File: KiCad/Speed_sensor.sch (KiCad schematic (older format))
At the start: 69 parts, among them J1 USB_B_Micro, J2 SWD, U1 BQ24040DSQR, U2 TP1941U, U3 ST1PS02, U4 nRF52832-QFxx, U5 LIS2DH12, Y1 32,768kHz, Y2 32MHz

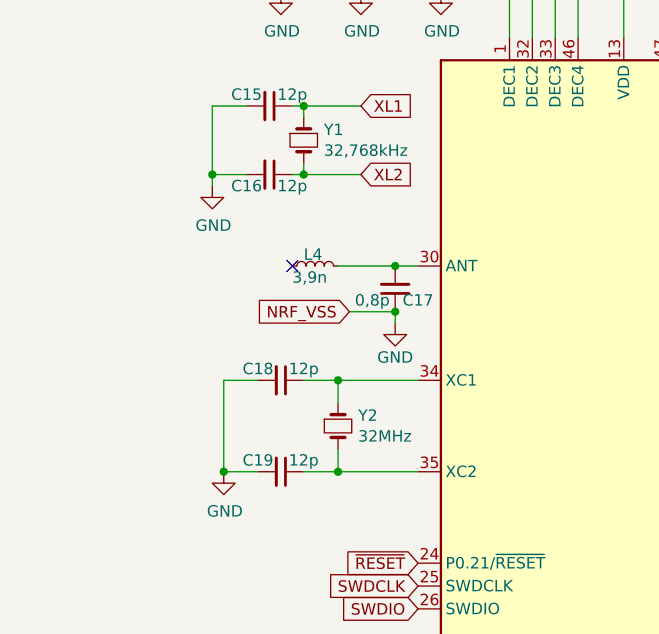
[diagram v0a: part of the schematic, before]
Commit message: added all footprints (LFO crystal might have to be updated)
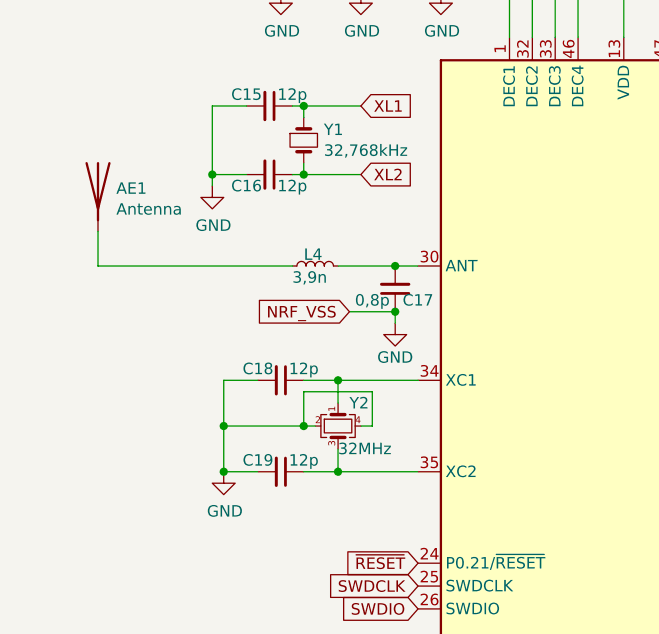
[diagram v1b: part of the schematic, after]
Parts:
- removed Y2: 32MHz, symbol Device:Crystal_Small
- added AE1: Antenna, RF_Antenna:Texas_SWRA117D_2.4GHz_Right, symbol Device:Antenna
- added Y2: 32MHz, Crystal:Crystal_SMD_2016-4Pin_2.0x1.6mm, symbol Device:Crystal_GND24_Small
- U1: footprint (none) -> Package_WSON-10:BQ24040DSQR_breitePins
- U2: footprint (none) -> Package_TO_SOT_SMD:SOT-23-5_HandSoldering
- U3: footprint (none) -> Package_TQFN-12:ST1PS02CQTR_breitePins
- U5: footprint (none) -> Package_LGA:LGA-12_2x2mm_P0.5mm
- Y1: footprint (none) -> Crystal:Crystal_SMD_2012-2Pin_2.0x1.2mm_HandSoldering
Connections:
- net GND: now also Y2.2, Y2.4
- net at C18.1, U4.34 (XC1): now also Y2.1
- net at C19.1, U4.35 (XC2): now also Y2.3
- net at L4.1: now also AE1.1 (A)
- no-connect marks 23 -> 22
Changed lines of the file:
@@
 Wire Wire Line
 	2500 3100 2850 3100
-$Comp
-L Device:Crystal_Small Y2
-U 1 1 6084A82A
-P 1900 5850
-F 0 "Y2" V 1854 5938 50  0000 L CNN
-F 1 "32MHz" V 1945 5938 50  0000 L CNN
-F 2 "" H 1900 5850 50  0001 C CNN
-F 3 "~" H 1900 5850 50  0001 C CNN
-	1    1900 5850
-	0    1    1    0
-$EndComp
 Wire Wire Line
 	2250 5650 1900 5650
@@
 	1550 5650 1400 5650
 Wire Wire Line
-	1400 5650 1400 6050
+	1400 5650 1400 5850
 Connection ~ 1400 6050
 $Comp
@@
 F 0 "U2" H 7950 1550 50  0000 C CNN
 F 1 "TP1941U" H 8000 1150 50  0000 C CNN
-F 2 "" H 8100 1350 50  0001 C CNN
+F 2 "Package_TO_SOT_SMD:SOT-23-5_HandSoldering" H 8100 1350 50  0001 C CNN
 F 3 "" H 8100 1350 50  0001 C CNN
 	1    8050 1350
@@
 F 0 "U3" H 9900 1600 50  0000 L CNN
 F 1 "ST1PS02" H 9900 800 50  0000 L CNN
-F 2 "" H 10150 1100 50  0001 C CNN
+F 2 "Package_TQFN-12:ST1PS02CQTR_breitePins" H 10150 1100 50  0001 C CNN
 F 3 "" H 10150 1100 50  0001 C CNN
 	1    10050 1200
@@
 F 0 "U1" H 3575 1915 50  0000 C CNN
 F 1 "BQ24040DSQR" H 3575 1824 50  0000 C CNN
-F 2 "" H 3550 1400 50  0001 C CNN
+F 2 "Package_WSON-10:BQ24040DSQR_breitePins" H 3550 1400 50  0001 C CNN
 F 3 "" H 3550 1400 50  0001 C CNN
 	1    3550 1400
@@
 F 0 "Y1" V 1704 4688 50  0000 L CNN
 F 1 "32,768kHz" V 1795 4688 50  0000 L CNN
-F 2 "" H 1750 4600 50  0001 C CNN
+F 2 "Crystal:Crystal_SMD_2012-2Pin_2.0x1.2mm_HandSoldering" H 1750 4600 50  0001 C CNN
 F 3 "~" H 1750 4600 50  0001 C CNN
 	1    1750 4600
@@
 F 0 "U5" H 7300 4750 50  0000 L CNN
 F 1 "LIS2DH12" H 7650 4750 50  0000 L CNN
-F 2 "" H 7550 4400 25  0001 C CNN
+F 2 "Package_LGA:LGA-12_2x2mm_P0.5mm" H 7550 4400 25  0001 C CNN
 F 3 "" H 7550 4400 25  0001 C CNN
 	1    7550 4400
@@
 Wire Wire Line
 	9000 1000 9000 1050
-NoConn ~ 1700 5150
 Wire Wire Line
 	3150 3050 3150 3100
@@
 Wire Wire Line
 	3150 3100 3150 4150
+$Comp
+L Device:Crystal_GND24_Small Y2
+U 1 1 6096B8F0
+P 1900 5850
+F 0 "Y2" V 1800 5900 50  0000 L CNN
+F 1 "32MHz" V 2000 5850 50  0000 L CNN
+F 2 "Crystal:Crystal_SMD_2016-4Pin_2.0x1.6mm" H 1900 5850 50  0001 C CNN
+F 3 "~" H 1900 5850 50  0001 C CNN
+	1    1900 5850
+	0    1    1    0
+$EndComp
+Wire Wire Line
+	1800 5850 1750 5850
+Connection ~ 1400 5850
+Wire Wire Line
+	1400 5850 1400 6050
+Connection ~ 1750 5850
+Wire Wire Line
+	1750 5850 1400 5850
+Wire Wire Line
+	1750 5700 1750 5850
+Wire Wire Line
+	2000 5850 2050 5850
+Wire Wire Line
+	2050 5850 2050 5700
+Wire Wire Line
+	1750 5700 2050 5700
+$Comp
+L Device:Antenna AE1
+U 1 1 6099647A
+P 850 4800
+F 0 "AE1" H 930 4789 50  0000 L CNN
+F 1 "Antenna" H 930 4698 50  0000 L CNN
+F 2 "RF_Antenna:Texas_SWRA117D_2.4GHz_Right" H 850 4800 50  0001 C CNN
+F 3 "~" H 850 4800 50  0001 C CNN
+	1    850  4800
+	1    0    0    -1
+$EndComp
+Wire Wire Line
+	850  5000 850  5150
+Wire Wire Line
+	850  5150 1700 5150
 $EndSCHEMATC

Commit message: custom footprints von Manu übernommen (jetzt sollte alles passen), PCB layout angefangen.
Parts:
- U4: footprint Package_DFN_QFN:QFN-48-1EP_6x6mm_P0.4mm_EP4.6x4.6mm -> myparts:QFN-48-1EP_6x6mm_P0.4mm_EP4.6x4.6mm_Handsolder
- U5: footprint Package_LGA:LGA-12_2x2mm_P0.5mm -> myparts:LGA-12_2x2mm_P0.5mm_Handsolder
- Y1: footprint Crystal:Crystal_SMD_2012-2Pin_2.0x1.2mm_HandSoldering -> myparts:TestPoint_2Pads_Pitch1mm_Drill0.4mm
- Y2: footprint Crystal:Crystal_SMD_2016-4Pin_2.0x1.6mm -> myparts:SMD-2016_4P
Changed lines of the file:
@@
 F 0 "U4" H 3850 7550 50  0000 C CNN
 F 1 "nRF52832-QFxx" H 3550 4200 50  0000 C CNN
-F 2 "Package_DFN_QFN:QFN-48-1EP_6x6mm_P0.4mm_EP4.6x4.6mm" H 3150 3750 50  0001 C CNN
+F 2 "myparts:QFN-48-1EP_6x6mm_P0.4mm_EP4.6x4.6mm_Handsolder" H 3150 3750 50  0001 C CNN
 F 3 "http://infocenter.nordicsemi.com/pdf/nRF52832_PS_v1.4.pdf" H 2650 6050 50  0001 C CNN
 	1    3150 5850
@@
 F 0 "Y1" V 1704 4688 50  0000 L CNN
 F 1 "32,768kHz" V 1795 4688 50  0000 L CNN
-F 2 "Crystal:Crystal_SMD_2012-2Pin_2.0x1.2mm_HandSoldering" H 1750 4600 50  0001 C CNN
+F 2 "myparts:TestPoint_2Pads_Pitch1mm_Drill0.4mm" H 1750 4600 50  0001 C CNN
 F 3 "~" H 1750 4600 50  0001 C CNN
 	1    1750 4600
@@
 F 0 "U5" H 7300 4750 50  0000 L CNN
 F 1 "LIS2DH12" H 7650 4750 50  0000 L CNN
-F 2 "Package_LGA:LGA-12_2x2mm_P0.5mm" H 7550 4400 25  0001 C CNN
+F 2 "myparts:LGA-12_2x2mm_P0.5mm_Handsolder" H 7550 4400 25  0001 C CNN
 F 3 "" H 7550 4400 25  0001 C CNN
 	1    7550 4400
@@
 F 0 "Y2" V 1800 5900 50  0000 L CNN
 F 1 "32MHz" V 2000 5850 50  0000 L CNN
-F 2 "Crystal:Crystal_SMD_2016-4Pin_2.0x1.6mm" H 1900 5850 50  0001 C CNN
+F 2 "myparts:SMD-2016_4P" H 1900 5850 50  0001 C CNN
 F 3 "~" H 1900 5850 50  0001 C CNN
 	1    1900 5850

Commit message: layout. parts roughly put into the right spot
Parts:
- removed C3: 1u, Capacitor_SMD:C_0603_1608Metric_Pad1.08x0.95mm_HandSolder, symbol Device:C_Small
- renumbered C4 to C3, C5 to C4
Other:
- note added: "R10 kann evtl. entfernt werden."
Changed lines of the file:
@@
-$Comp
-L Device:C_Small C?
-U 1 1 609A977E
-P 6500 1300
-AR Path="/608A57BF/609A977E" Ref="C?"  Part="1"
-AR Path="/609A977E" Ref="C3"  Part="1"
-F 0 "C3" H 6350 1350 50  0000 L CNN
-F 1 "1u" H 6350 1250 50  0000 L CNN
-F 2 "Capacitor_SMD:C_0603_1608Metric_Pad1.08x0.95mm_HandSolder" H 6500 1300 50  0001 C CNN
-F 3 "~" H 6500 1300 50  0001 C CNN
-	1    6500 1300
-	1    0    0    -1
-$EndComp
 $Comp
 L Device:C_Small C?
@@
 P 6650 1300
 AR Path="/608A57BF/609A9B57" Ref="C?"  Part="1"
-AR Path="/609A9B57" Ref="C4"  Part="1"
-F 0 "C4" H 6742 1346 50  0000 L CNN
+AR Path="/609A9B57" Ref="C3"  Part="1"
+F 0 "C3" H 6742 1346 50  0000 L CNN
 F 1 "100n" H 6742 1255 50  0000 L CNN
 F 2 "Capacitor_SMD:C_0603_1608Metric_Pad1.08x0.95mm_HandSolder" H 6650 1300 50  0001 C CNN
@@
 $EndComp
 Wire Wire Line
-	6500 1200 6650 1200
-Wire Wire Line
 	6650 1200 6650 1100
-Connection ~ 6650 1200
-Wire Wire Line
-	6500 1400 6650 1400
 Wire Wire Line
 	6650 1400 6650 1500
-Connection ~ 6650 1400
 Text Notes 8950 600  0    50   ~ 0
 Buck converter
@@
 P 9000 1150
 AR Path="/608A57BF/60A48461" Ref="C?"  Part="1"
-AR Path="/60A48461" Ref="C5"  Part="1"
-F 0 "C5" H 9092 1196 50  0000 L CNN
+AR Path="/60A48461" Ref="C4"  Part="1"
+F 0 "C4" H 9092 1196 50  0000 L CNN
 F 1 "10u" H 9092 1105 50  0000 L CNN
 F 2 "Capacitor_SMD:C_0603_1608Metric_Pad1.08x0.95mm_HandSolder" H 9000 1150 50  0001 C CNN
@@
 Wire Wire Line
 	850  5150 1700 5150
+Text Notes 10550 1800 0    25   ~ 0
+R10 kann evtl. entfernt werden.
 $EndSCHEMATC

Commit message: played around with part positioning slightly
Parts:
- removed AE1: Antenna, RF_Antenna:Texas_SWRA117D_2.4GHz_Right, symbol Device:Antenna
- removed H2: Vout2, TestPoint:TestPoint_Plated_Hole_D2.0mm, symbol Mechanical:MountingHole_Pad
- added AE1: 2,4GHz, RF_Antenna:Texas_SWRA117D_2.4GHz_Right, symbol Device:Antenna_Shield
- added C5: 100n, Capacitor_SMD:C_0402_1005Metric_Pad0.74x0.62mm_HandSolder, symbol Device:C_Small
- H1, H10, H11, H12, H3, H4, H5, H6, H7, H8, H9: footprint TestPoint:TestPoint_Plated_Hole_D2.0mm -> TestPoint:TestPoint_Loop_D1.80mm_Drill1.0mm_Beaded
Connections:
- net +3V0: now also C5.1
- net GND: now also AE1.2 (Shield), C5.2
- net at L4.1: now also AE1.1 (A)
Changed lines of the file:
@@
 Text GLabel 10450 3750 0    50   Input ~ 0
 BUCK_VOUT
-Text GLabel 10450 3900 0    50   Input ~ 0
-BUCK_Vout2
 Text GLabel 4050 5650 2    50   Input ~ 0
 SPI_01_CS
@@
 F 0 "H1" V 10504 3900 50  0000 L CNN
 F 1 "VOUT" V 10595 3900 50  0000 L CNN
-F 2 "TestPoint:TestPoint_Plated_Hole_D2.0mm" H 10550 3750 50  0001 C CNN
+F 2 "TestPoint:TestPoint_Loop_D1.80mm_Drill1.0mm_Beaded" H 10550 3750 50  0001 C CNN
 F 3 "~" H 10550 3750 50  0001 C CNN
 	1    10550 3750
@@
 U 1 1 60AF63B1
 P 6350 4400
-F 0 "C20" H 6150 4450 50  0000 L CNN
-F 1 "100n" H 6100 4350 50  0000 L CNN
+F 0 "C20" H 6250 4500 50  0000 L CNN
+F 1 "100n" H 6200 4300 50  0000 L CNN
 F 2 "Capacitor_SMD:C_0402_1005Metric_Pad0.74x0.62mm_HandSolder" H 6350 4400 50  0001 C CNN
 F 3 "~" H 6350 4400 50  0001 C CNN
@@
 F 0 "H5" V 9254 3900 50  0000 L CNN
 F 1 "AIN0" V 9345 3900 50  0000 L CNN
-F 2 "TestPoint:TestPoint_Plated_Hole_D2.0mm" H 9300 3750 50  0001 C CNN
+F 2 "TestPoint:TestPoint_Loop_D1.80mm_Drill1.0mm_Beaded" H 9300 3750 50  0001 C CNN
 F 3 "~" H 9300 3750 50  0001 C CNN
 	1    9300 3750
@@
 F 0 "H6" V 9254 4050 50  0000 L CNN
 F 1 "AIN1" V 9345 4050 50  0000 L CNN
-F 2 "TestPoint:TestPoint_Plated_Hole_D2.0mm" H 9300 3900 50  0001 C CNN
+F 2 "TestPoint:TestPoint_Loop_D1.80mm_Drill1.0mm_Beaded" H 9300 3900 50  0001 C CNN
 F 3 "~" H 9300 3900 50  0001 C CNN
 	1    9300 3900
@@
 F 0 "H7" V 9254 4200 50  0000 L CNN
 F 1 "AIN2" V 9345 4200 50  0000 L CNN
-F 2 "TestPoint:TestPoint_Plated_Hole_D2.0mm" H 9300 4050 50  0001 C CNN
+F 2 "TestPoint:TestPoint_Loop_D1.80mm_Drill1.0mm_Beaded" H 9300 4050 50  0001 C CNN
 F 3 "~" H 9300 4050 50  0001 C CNN
 	1    9300 4050
@@
 F 0 "H8" V 9254 4350 50  0000 L CNN
 F 1 "AIN3" V 9345 4350 50  0000 L CNN
-F 2 "TestPoint:TestPoint_Plated_Hole_D2.0mm" H 9300 4200 50  0001 C CNN
+F 2 "TestPoint:TestPoint_Loop_D1.80mm_Drill1.0mm_Beaded" H 9300 4200 50  0001 C CNN
 F 3 "~" H 9300 4200 50  0001 C CNN
 	1    9300 4200
@@
 F 0 "H9" V 9254 4500 50  0000 L CNN
 F 1 "AIN4" V 9345 4500 50  0000 L CNN
-F 2 "TestPoint:TestPoint_Plated_Hole_D2.0mm" H 9300 4350 50  0001 C CNN
+F 2 "TestPoint:TestPoint_Loop_D1.80mm_Drill1.0mm_Beaded" H 9300 4350 50  0001 C CNN
 F 3 "~" H 9300 4350 50  0001 C CNN
 	1    9300 4350
@@
 F 0 "H10" V 9254 4650 50  0000 L CNN
 F 1 "AIN5" V 9345 4650 50  0000 L CNN
-F 2 "TestPoint:TestPoint_Plated_Hole_D2.0mm" H 9300 4500 50  0001 C CNN
+F 2 "TestPoint:TestPoint_Loop_D1.80mm_Drill1.0mm_Beaded" H 9300 4500 50  0001 C CNN
 F 3 "~" H 9300 4500 50  0001 C CNN
 	1    9300 4500
@@
 F 0 "H11" V 9250 4800 50  0000 L CNN
 F 1 "AIN6" V 9345 4800 50  0000 L CNN
-F 2 "TestPoint:TestPoint_Plated_Hole_D2.0mm" H 9300 4650 50  0001 C CNN
+F 2 "TestPoint:TestPoint_Loop_D1.80mm_Drill1.0mm_Beaded" H 9300 4650 50  0001 C CNN
 F 3 "~" H 9300 4650 50  0001 C CNN
 	1    9300 4650
@@
 F 0 "H12" V 9254 4950 50  0000 L CNN
 F 1 "AIN7" V 9345 4950 50  0000 L CNN
-F 2 "TestPoint:TestPoint_Plated_Hole_D2.0mm" H 9300 4800 50  0001 C CNN
+F 2 "TestPoint:TestPoint_Loop_D1.80mm_Drill1.0mm_Beaded" H 9300 4800 50  0001 C CNN
 F 3 "~" H 9300 4800 50  0001 C CNN
 	1    9300 4800
@@
 F 0 "H4" V 10504 4350 50  0000 L CNN
 F 1 "SPI_01_CSB" V 10595 4350 50  0000 L CNN
-F 2 "TestPoint:TestPoint_Plated_Hole_D2.0mm" H 10550 4200 50  0001 C CNN
+F 2 "TestPoint:TestPoint_Loop_D1.80mm_Drill1.0mm_Beaded" H 10550 4200 50  0001 C CNN
 F 3 "~" H 10550 4200 50  0001 C CNN
 	1    10550 4200
@@
 F 0 "H3" V 10504 4200 50  0000 L CNN
 F 1 "PGOOD" V 10595 4200 50  0000 L CNN
-F 2 "TestPoint:TestPoint_Plated_Hole_D2.0mm" H 10550 4050 50  0001 C CNN
+F 2 "TestPoint:TestPoint_Loop_D1.80mm_Drill1.0mm_Beaded" H 10550 4050 50  0001 C CNN
 F 3 "~" H 10550 4050 50  0001 C CNN
 	1    10550 4050
-	0    1    1    0
-$EndComp
-$Comp
-L Mechanical:MountingHole_Pad H2
-U 1 1 609B3292
-P 10550 3900
-F 0 "H2" V 10504 4050 50  0000 L CNN
-F 1 "Vout2" V 10595 4050 50  0000 L CNN
-F 2 "TestPoint:TestPoint_Plated_Hole_D2.0mm" H 10550 3900 50  0001 C CNN
-F 3 "~" H 10550 3900 50  0001 C CNN
-	1    10550 3900
 	0    1    1    0
 $EndComp
@@
 Wire Wire Line
 	1750 5700 2050 5700
-$Comp
-L Device:Antenna AE1
-U 1 1 6099647A
-P 850 4800
-F 0 "AE1" H 930 4789 50  0000 L CNN
-F 1 "Antenna" H 930 4698 50  0000 L CNN
-F 2 "RF_Antenna:Texas_SWRA117D_2.4GHz_Right" H 850 4800 50  0001 C CNN
-F 3 "~" H 850 4800 50  0001 C CNN
-	1    850  4800
-	1    0    0    -1
-$EndComp
 Wire Wire Line
 	850  5000 850  5150
@@
 Text Notes 10550 1800 0    25   ~ 0
 R10 kann evtl. entfernt werden.
+$Comp
+L Device:Antenna_Shield AE1
+U 1 1 608E3518
+P 850 4800
+F 0 "AE1" H 770 4839 50  0000 R CNN
+F 1 "2,4GHz" H 770 4748 50  0000 R CNN
+F 2 "RF_Antenna:Texas_SWRA117D_2.4GHz_Right" H 850 4900 50  0001 C CNN
+F 3 "~" H 850 4900 50  0001 C CNN
+	1    850  4800
+	-1   0    0    -1
+$EndComp
+$Comp
+L power:GND #PWR035
+U 1 1 608ED256
+P 750 5000
+F 0 "#PWR035" H 750 4750 50  0001 C CNN
+F 1 "GND" H 755 4827 50  0000 C CNN
+F 2 "" H 750 5000 50  0001 C CNN
+F 3 "" H 750 5000 50  0001 C CNN
+	1    750  5000
+	1    0    0    -1
+$EndComp
+$Comp
+L Device:C_Small C5
+U 1 1 6094D484
+P 6200 4400
+F 0 "C5" H 6000 4450 50  0000 L CNN
+F 1 "100n" H 5950 4350 50  0000 L CNN
+F 2 "Capacitor_SMD:C_0402_1005Metric_Pad0.74x0.62mm_HandSolder" H 6200 4400 50  0001 C CNN
+F 3 "~" H 6200 4400 50  0001 C CNN
+	1    6200 4400
+	1    0    0    -1
+$EndComp
+Wire Wire Line
+	6350 4250 6200 4250
+Wire Wire Line
+	6200 4250 6200 4300
+Wire Wire Line
+	6200 4500 6200 4550
+Wire Wire Line
+	6200 4550 6350 4550
 $EndSCHEMATC

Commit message: small changes in the layout
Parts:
- removed AE1: 2,4GHz, RF_Antenna:Texas_SWRA117D_2.4GHz_Right, symbol Device:Antenna_Shield
- added AE1: 2450AT18D0100E, myparts:2450AT18D0100E, symbol myparts:2450AT18D0100E
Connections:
- net GND: now also AE1.2 (GND), AE1.3 (GND), AE1.4 (GND)
- net at L4.1: now also AE1.1 (FEED)
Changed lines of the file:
@@
 Wire Wire Line
 	1750 5700 2050 5700
-Wire Wire Line
-	850  5000 850  5150
-Wire Wire Line
-	850  5150 1700 5150
 Text Notes 10550 1800 0    25   ~ 0
 R10 kann evtl. entfernt werden.
-$Comp
-L Device:Antenna_Shield AE1
-U 1 1 608E3518
-P 850 4800
-F 0 "AE1" H 770 4839 50  0000 R CNN
-F 1 "2,4GHz" H 770 4748 50  0000 R CNN
-F 2 "RF_Antenna:Texas_SWRA117D_2.4GHz_Right" H 850 4900 50  0001 C CNN
-F 3 "~" H 850 4900 50  0001 C CNN
-	1    850  4800
-	-1   0    0    -1
-$EndComp
-$Comp
-L power:GND #PWR035
-U 1 1 608ED256
-P 750 5000
-F 0 "#PWR035" H 750 4750 50  0001 C CNN
-F 1 "GND" H 755 4827 50  0000 C CNN
-F 2 "" H 750 5000 50  0001 C CNN
-F 3 "" H 750 5000 50  0001 C CNN
-	1    750  5000
-	1    0    0    -1
-$EndComp
 $Comp
 L Device:C_Small C5
@@
 Wire Wire Line
 	6200 4550 6350 4550
+$Comp
+L myparts:2450AT18D0100E AE1
+U 1 1 6099F4A4
+P 1000 5450
+F 0 "AE1" H 1050 5250 60  0000 C CNN
+F 1 "2450AT18D0100E" H 1000 5550 60  0000 C CNN
+F 2 "myparts:2450AT18D0100E" H 1150 5400 60  0001 C CNN
+F 3 "" H 1300 5450 60  0001 C CNN
+	1    1000 5450
+	0    1    1    0
+$EndComp
+Wire Wire Line
+	1000 5150 1700 5150
+$Comp
+L power:GND #PWR035
+U 1 1 609D15A8
+P 700 5150
+F 0 "#PWR035" H 700 4900 50  0001 C CNN
+F 1 "GND" H 705 4977 50  0000 C CNN
+F 2 "" H 700 5150 50  0001 C CNN
+F 3 "" H 700 5150 50  0001 C CNN
+	1    700  5150
+	1    0    0    -1
+$EndComp
+Wire Wire Line
+	700  5150 900  5150
+$Comp
+L power:GND #PWR036
+U 1 1 609D8BDF
+P 700 5800
+F 0 "#PWR036" H 700 5550 50  0001 C CNN
+F 1 "GND" H 705 5627 50  0000 C CNN
+F 2 "" H 700 5800 50  0001 C CNN
+F 3 "" H 700 5800 50  0001 C CNN
+	1    700  5800
+	1    0    0    -1
+$EndComp
+Wire Wire Line
+	1000 5800 900  5800
+Connection ~ 900  5800
+Wire Wire Line
+	900  5800 700  5800
 $EndSCHEMATC

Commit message: layout part placement (again, very small changes)
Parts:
- Y1: footprint myparts:TestPoint_2Pads_Pitch1mm_Drill0.4mm -> Crystal:Crystal_SMD_G8-2Pin_3.2x1.5mm
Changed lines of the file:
@@
 	1    0    0    -1
 $EndComp
-Text GLabel 4000 1150 2    50   Input ~ 0
+Text GLabel 4100 1100 2    50   Input ~ 0
 BQ_OUT
 Text GLabel 4000 1250 2    50   Input ~ 0
@@
 F 0 "Y1" V 1704 4688 50  0000 L CNN
 F 1 "32,768kHz" V 1795 4688 50  0000 L CNN
-F 2 "myparts:TestPoint_2Pads_Pitch1mm_Drill0.4mm" H 1750 4600 50  0001 C CNN
+F 2 "Crystal:Crystal_SMD_G8-2Pin_3.2x1.5mm" H 1750 4600 50  0001 C CNN
 F 3 "~" H 1750 4600 50  0001 C CNN
 	1    1750 4600
@@
 Wire Wire Line
 	900  5800 700  5800
+Wire Wire Line
+	4100 1100 4100 1150
+Wire Wire Line
+	4100 1150 4000 1150
 $EndSCHEMATC
